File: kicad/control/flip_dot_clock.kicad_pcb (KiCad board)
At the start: 4 copper layers, 140.2 x 46.1 mm, 33 parts, among them U1 NUCLEO-F303K8-HEADER, U10 Small_7_Seg_FlipDot_Module, U2 SLC03B-05, U3 NCV7719, U4 Small_7_Seg_FlipDot_Module, U5 NCV7719, U6 Small_7_Seg_FlipDot_Module, U7 NCV7719, U8 Small_7_Seg_FlipDot_Module, U9 NCV7719

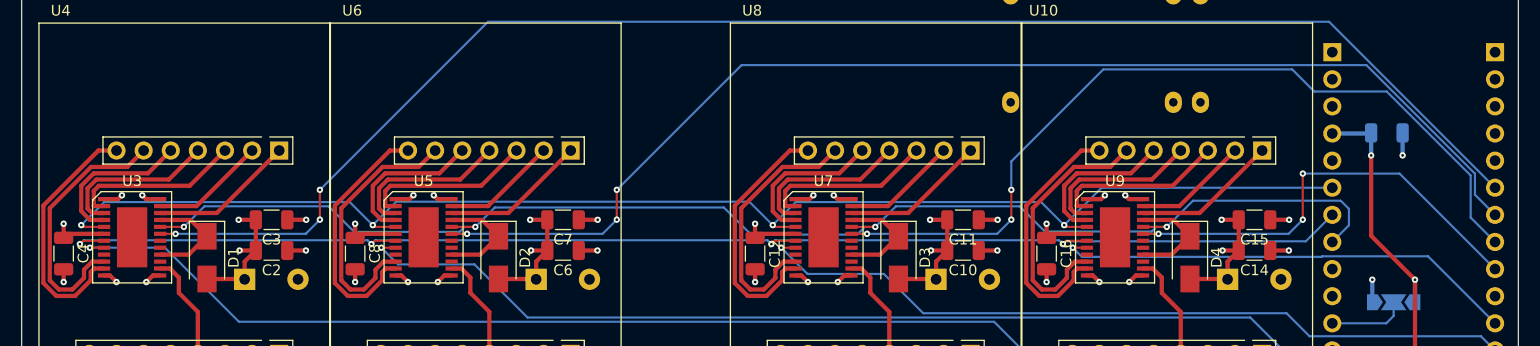
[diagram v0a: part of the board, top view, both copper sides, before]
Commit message: update power planes, move C17, update EN pin mux
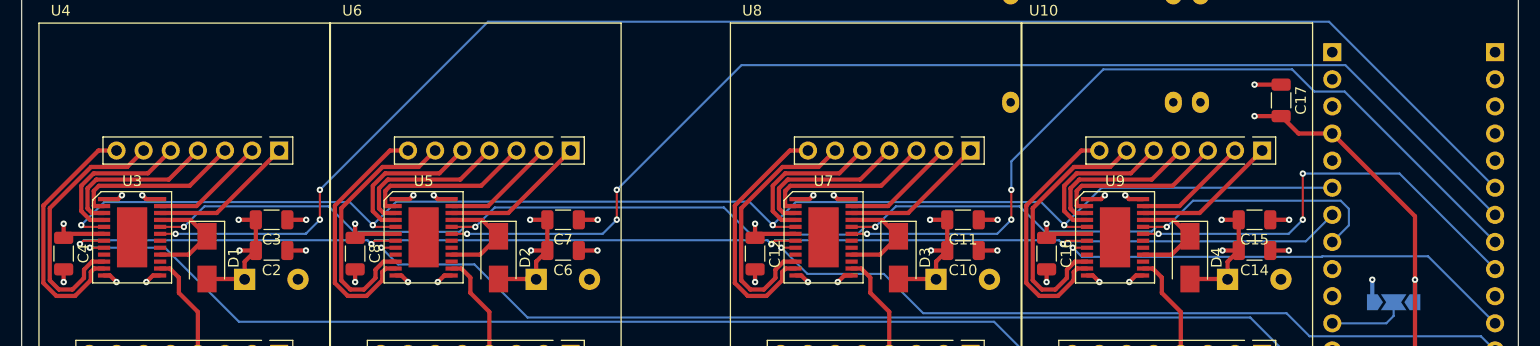
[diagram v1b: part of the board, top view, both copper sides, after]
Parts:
- C17: moved to F.Cu
- moved C17 10.4 mm to (196.7, 86.1), turned to -90 degrees
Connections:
- C17 pad 1: +5V -> GND
- C17 pad 2: GND -> +5V
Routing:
- net +5V: track 54.2 -> 60.0 mm
- net /SPI1_CS_3: track 78.9 -> 76.6 mm
- net /SPI1_CS_2: track 112.9 -> 111.7 mm

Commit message: DRC updates
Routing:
- net /F_SET_1: track 24.8 -> 20.0 mm
- net /F_SET_2: track 24.8 -> 20.0 mm
- net /F_SET_3: track 24.8 -> 20.0 mm
- net /F_SET_4: track 24.8 -> 20.0 mm
- net /G_SET_1: track 23.9 -> 19.2 mm
- net /G_SET_4: track 23.9 -> 19.2 mm
- net /G_SET_3: track 23.9 -> 19.2 mm
- net /G_SET_2: track 23.9 -> 19.2 mm

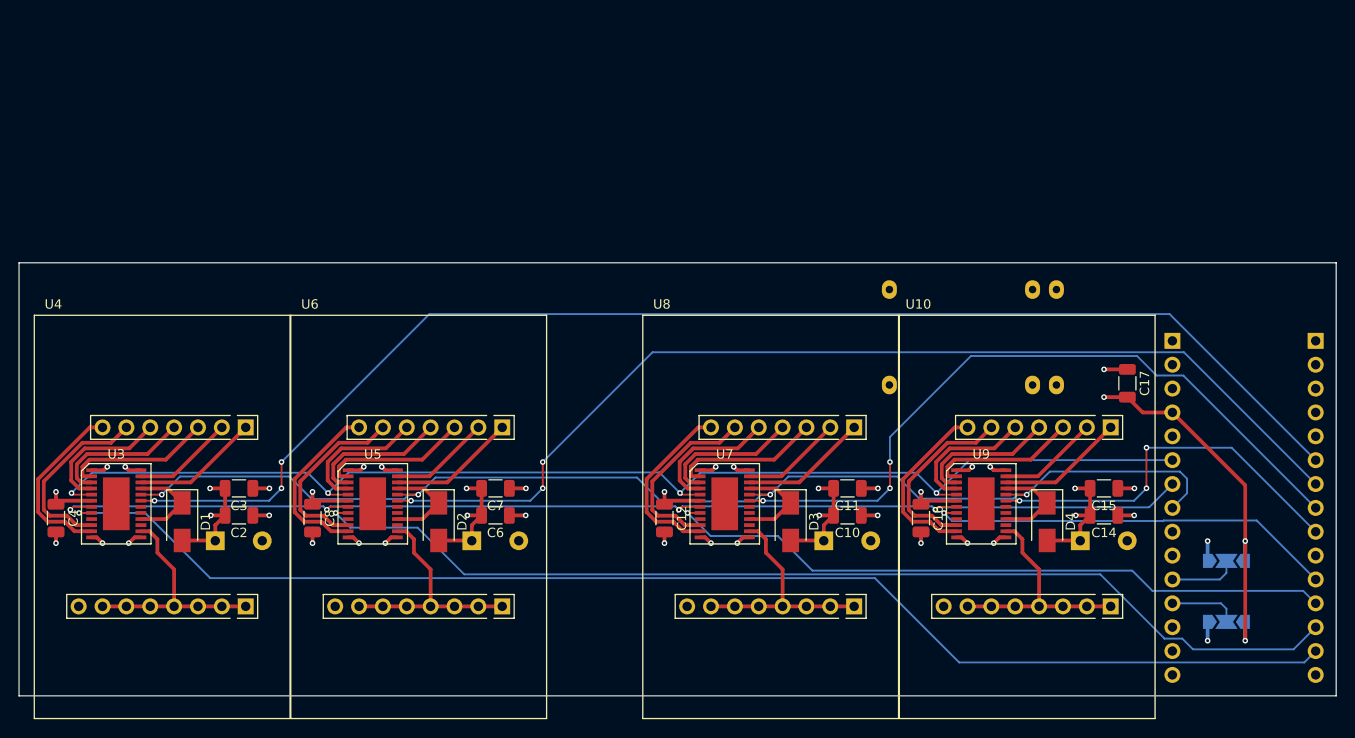
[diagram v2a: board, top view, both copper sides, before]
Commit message: update layout, add power connector
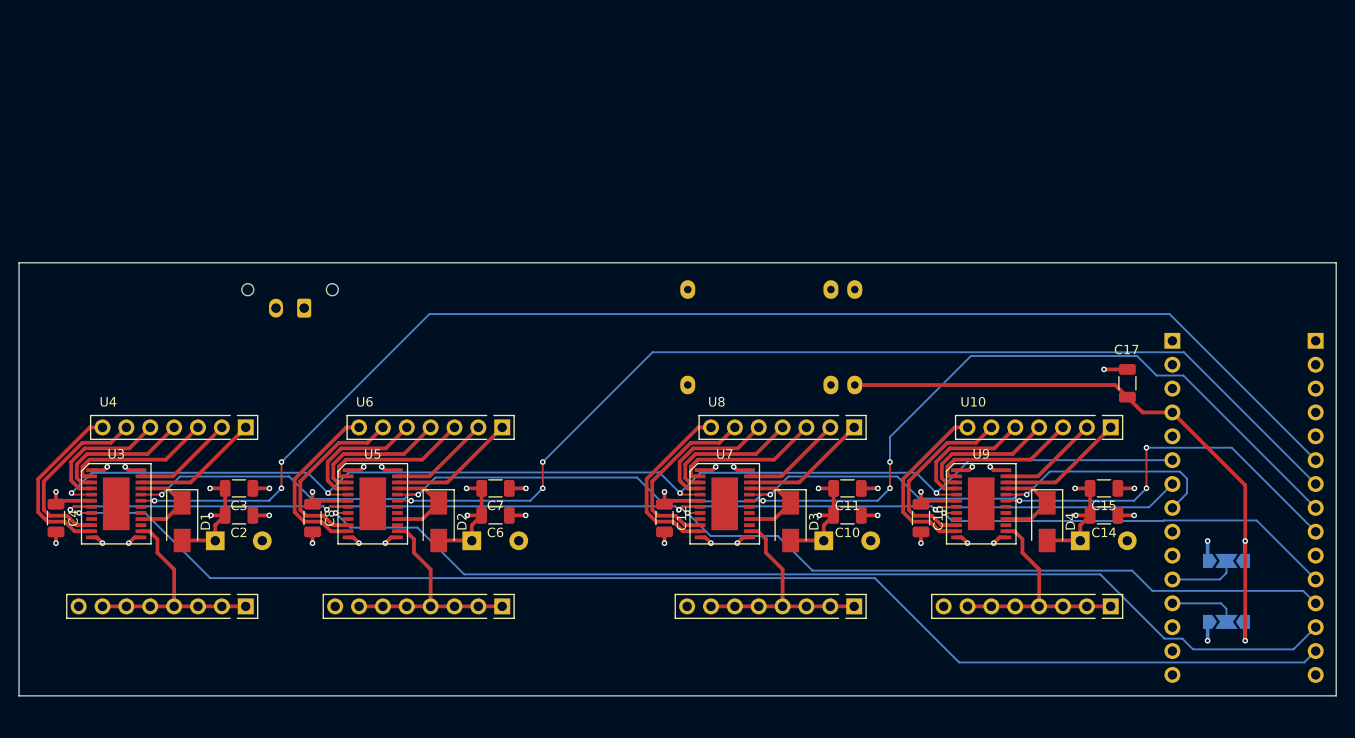
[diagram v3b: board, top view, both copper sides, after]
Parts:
- added J1: Conn_01x02_Male, Connector_Molex:Molex_Micro-Fit_3.0_43650-0215_1x02_P3.00mm_Vertical, B.Cu at (109.1, 78.1)
- moved U2 21.5 mm to (147.8, 74.4)
- turned C17 to 90 degrees
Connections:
- C17 pad 1: GND -> +5V
- C17 pad 2: +5V -> GND
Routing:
- net +5V: track 60.0 -> 87.0 mm, vias 7 -> 6

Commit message: updates
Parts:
- JP1, JP2: value SB -> SJ2O; footprint Jumper:SolderJumper-3_P2.0mm_Open_TrianglePad1.0x1.5mm_NumberLabels -> Jumper:SolderJumper-2_P1.3mm_Open_TrianglePad1.0x1.5mm
- moved JP1 2.69 mm to (209.2, 109.6)
- moved JP2 2.69 mm to (209.2, 106.9)
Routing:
- net +5V: track 87.0 -> 79.3 mm, vias 6 -> 5
- net GND: track 51.9 -> 47.8 mm, vias 31 -> 29
- net /SPI1_SCK: track 129.2 -> 125.8 mm
- net /SPI1_CS_3: track 76.6 -> 74.9 mm
- net /NCV_EN_3: track 72.2 -> 73.7 mm
- net /NCV_EN_2: track 112.7 -> 111.7 mm

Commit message: update pcb
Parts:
- moved J1 0.63 mm to (109.1, 78.7)
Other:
- board size 140.2 x 46.1 mm -> 139.7 x 45.7 mm
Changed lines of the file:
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@@
     )
     (pad_to_mask_clearance 0)
-    (grid_origin 78.74 119.38)
+    (grid_origin 79.248 119.38)
     (pcbplotparams
       (layerselection 0x00010f0_ffffffff)
@@
       (effects (font (size 1 1) (thickness 0.15)))
     )
-    (fp_text value "Small_7_Seg_FlipDot_Module" (at 12.7 -15.875) (layer "F.Fab")
+    (fp_text value "Small_7_Seg_FlipDot_Module" (at 12.573 -4.064) (layer "F.Fab")
       (effects (font (size 1 1) (thickness 0.15)))
     )
@@
       (effects (font (size 1 1) (thickness 0.15)))
     )
-    (fp_text value "Small_7_Seg_FlipDot_Module" (at 12.7 -15.875) (layer "F.Fab")
+    (fp_text value "Small_7_Seg_FlipDot_Module" (at 12.573 -4.064) (layer "F.Fab")
       (effects (font (size 1 1) (thickness 0.15)))
     )
@@
       (effects (font (size 1 1) (thickness 0.15)))
     )
-    (fp_text value "Small_7_Seg_FlipDot_Module" (at 12.7 -15.875) (layer "F.Fab")
+    (fp_text value "Small_7_Seg_FlipDot_Module" (at 12.573 -4.064) (layer "F.Fab")
       (effects (font (size 1 1) (thickness 0.15)))
     )
@@
       (effects (font (size 1 1) (thickness 0.15)))
     )
-    (fp_text value "Small_7_Seg_FlipDot_Module" (at 12.7 -15.875) (layer "F.Fab")
+    (fp_text value "Small_7_Seg_FlipDot_Module" (at 12.7 -4.191) (layer "F.Fab")
       (effects (font (size 1 1) (thickness 0.15)))
     )
@@
   )
   (footprint "Connector_Molex:Molex_Micro-Fit_3.0_43650-0215_1x02_P3.00mm_Vertical" (layer "B.Cu")
-    (at 109.093 78.105 180)
+    (at 109.093 78.74 180)
     (descr "Molex Micro-Fit 3.0 Connector System, 43650-0215 (compatible alternatives: 43650-0216, 43650-0217), 2 Pins per row (http://www.molex.com/pdm_docs/sd/436500215_sd.pdf), generated with kicad-footprint-generator")
     (tags "connector Molex Micro-Fit_3.0 vertical")
@@
     )
   )
-  (gr_line (start 78.74 119.38) (end 78.74 73.279)
+  (gr_line (start 79.248 119.38) (end 79.248 73.66)
     (stroke (width 0.05) (type solid)) (layer "Edge.Cuts"))
-  (gr_line (start 78.74 73.279) (end 218.948 73.279)
+  (gr_line (start 79.248 73.66) (end 218.948 73.66)
     (stroke (width 0.05) (type solid)) (layer "Edge.Cuts"))
-  (gr_line (start 218.948 119.38) (end 78.74 119.38)
+  (gr_line (start 218.948 119.38) (end 79.248 119.38)
     (stroke (width 0.05) (type solid)) (layer "Edge.Cuts"))
-  (gr_line (start 218.948 73.279) (end 218.948 119.38)
+  (gr_line (start 218.948 73.66) (end 218.948 119.38)
     (stroke (width 0.05) (type solid)) (layer "Edge.Cuts"))
+  (dimension (type aligned) (layer "Eco1.User")
+    (pts (xy 79.248 119.38) (xy 218.948 119.38))
+    (height 8.762999)
+    (gr_text "5500.0000  mils" (at 149.098 126.342999) (layer "Eco1.User")
+      (effects (font (size 1.5 1.5) (thickness 0.3)))
+    )
+    (format (units 3) (units_format 1) (precision 4))
+    (style (thickness 0.2) (arrow_length 1.27) (text_position_mode 0) (extension_height 0.58642) (extension_offset 0.5) keep_text_aligned)
+  )
+  (dimension (type aligned) (layer "Eco1.User")
+    (pts (xy 79.248 119.38) (xy 79.248 73.66))
+    (height -6.858)
+    (gr_text "1800.0000  mils" (at 70.59 96.52 90) (layer "Eco1.User")
+      (effects (font (size 1.5 1.5) (thickness 0.3)))
+    )
+    (format (units 3) (units_format 1) (precision 4))
+    (style (thickness 0.2) (arrow_length 1.27) (text_position_mode 0) (extension_height 0.58642) (extension_offset 0.5) keep_text_aligned)
+  )
   (segment (start 96.107 98.838) (end 94.577 97.308) (width 0.4) (layer "F.Cu") (net 1))
   (segment (start 96.107 98.838) (end 94.387 100.558) (width 0.4) (layer "F.Cu") (net 1))
@@
       (pts
         (xy 218.44 118.872)
-        (xy 79.248 118.872)
-        (xy 79.248 73.787)
-        (xy 218.44 73.787)
+        (xy 79.756 118.872)
+        (xy 79.756 74.168)
+        (xy 218.44 74.168)
       )
     )
@@
         (xy 86.106 94.996)
         (xy 86.106 99.441)
-        (xy 79.248 99.441)
-        (xy 79.248 90.043)
+        (xy 79.756 99.441)
+        (xy 79.756 90.043)
         (xy 86.106 90.043)
         (xy 86.106 92.329)
@@
       (pts
         (xy 218.44 118.872)
-        (xy 79.248 118.872)
-        (xy 79.248 100.076)
+        (xy 79.756 118.872)
+        (xy 79.756 100.076)
         (xy 86.741 100.076)
         (xy 86.741 95.631)
@@
         (xy 162.179 82.55)
         (xy 162.179 89.281)
-        (xy 79.248 89.408)
-        (xy 79.248 73.787)
-        (xy 166.751 73.787)
-        (xy 218.44 73.787)
+        (xy 79.756 89.408)
+        (xy 79.756 74.168)
+        (xy 218.44 74.168)
       )
     )

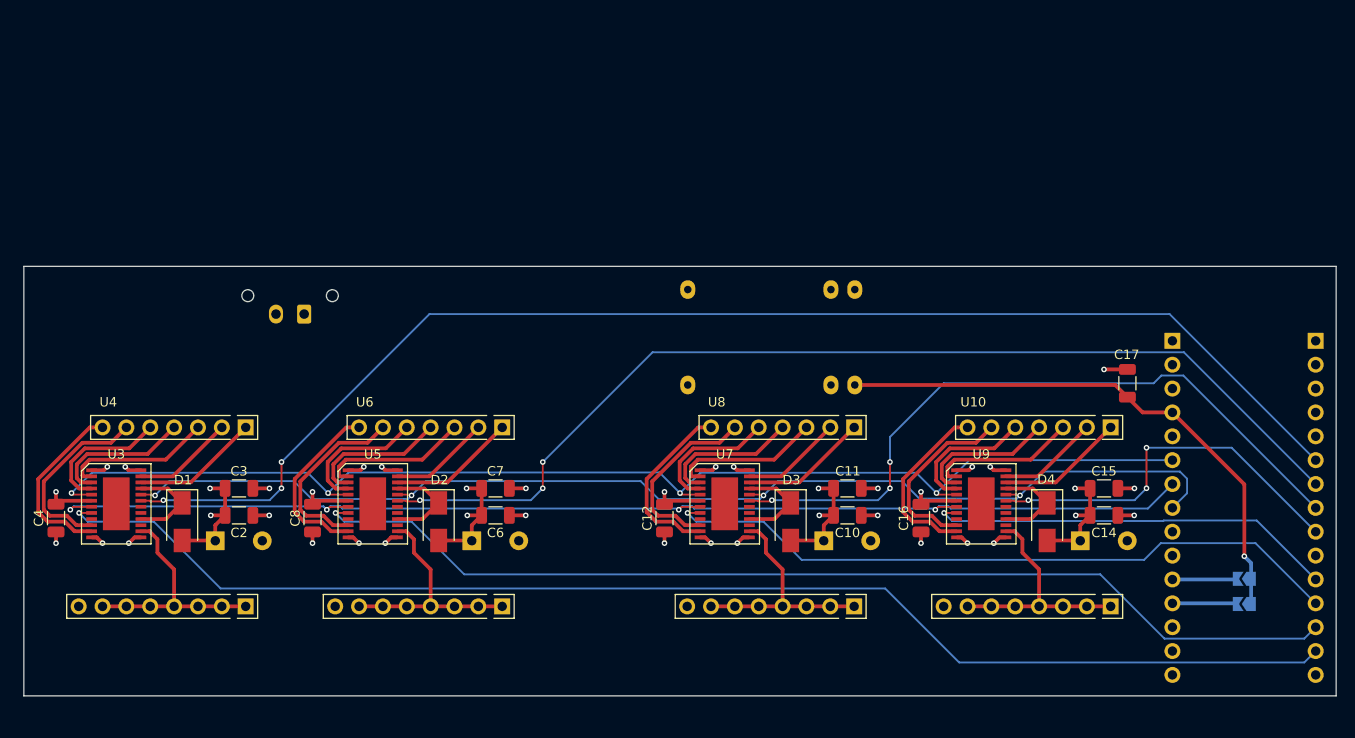
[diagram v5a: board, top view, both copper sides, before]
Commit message: begin PCB redesign based on overall clock dims
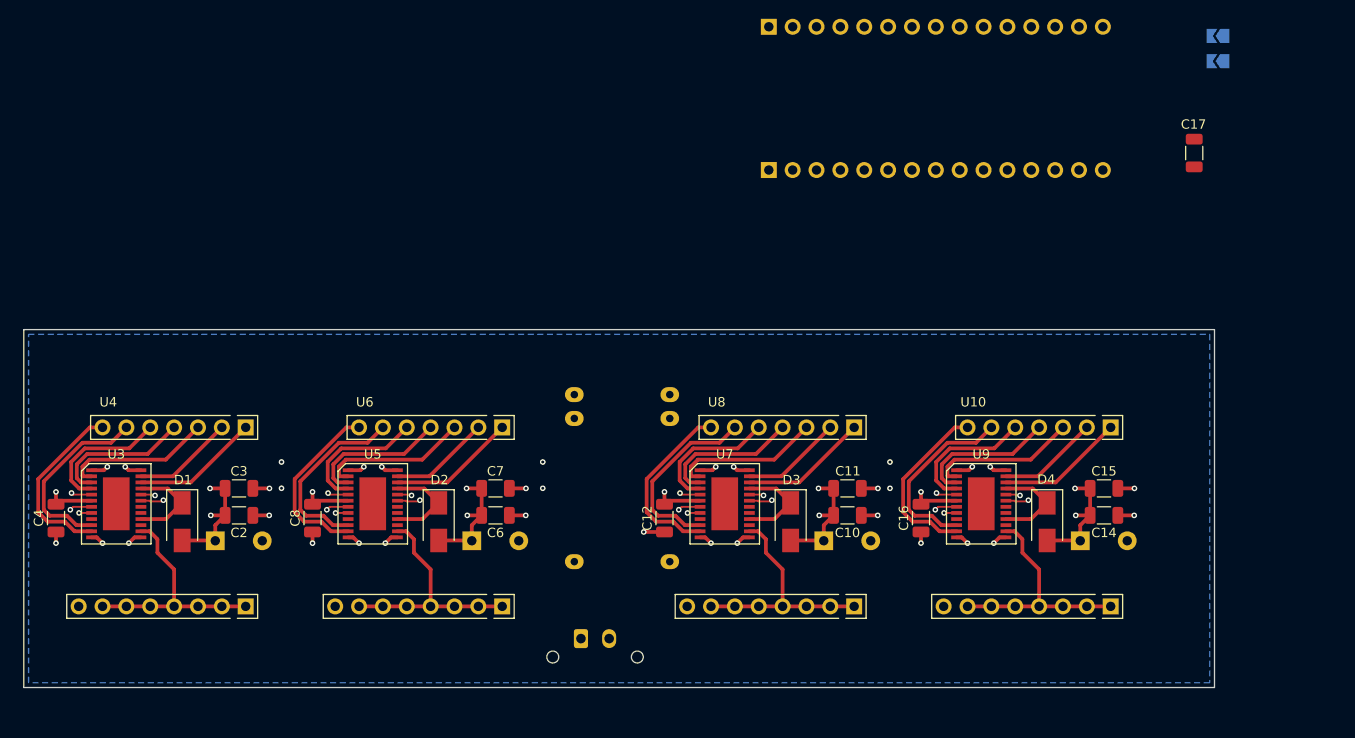
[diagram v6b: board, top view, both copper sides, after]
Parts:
- moved U1 78.9 mm to (200.2, 46.5), turned to -90 degrees
- moved JP2 57.9 mm to (206.4, 49.1)
- moved JP1 57.9 mm to (206.4, 51.8)
- moved J1 45.4 mm to (138.6, 113.3), turned to 0 degrees
- moved U2 34.9 mm to (136.1, 107.3), turned to 90 degrees
- moved C17 25.5 mm to (203.8, 61.6)
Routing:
- net +5V: track 79.3 -> 20.4 mm, vias 5 -> 4
- net /SPI1_CS_1: track 141.4 -> 86.7 mm
- net /SPI1_CS_2: track 111.8 -> 62.2 mm
- net /SPI1_CS_3: track 74.9 -> 26.7 mm
- net /NCV_EN_1: track 140.1 -> 99.4 mm
- net /SPI1_CS_4: track 41.6 -> 16.1 mm, vias 3 -> 1
- net /SPI1_MOSI: track 132.9 -> 115.1 mm
- net /NCV_EN_4: track 43.9 -> 30.8 mm
- net /SPI1_SCK: track 125.8 -> 116.2 mm
- net Net-(JP2-B): track 6.96 -> 0.10 mm
- net Net-(JP1-B): track 6.96 -> 0.10 mm
- net /NCV_EN_3: track 73.7 -> 68.7 mm
- net /SPI1_MISO: track 129.2 -> 131.6 mm
- net GND: track 47.8 -> 46.3 mm, vias 29 -> 28
- net /NCV_EN_2: track 111.7 -> 110.3 mm
- added copper zone on B.Cu, net GND
- removed copper zone on In1.Cu, net GND
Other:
- board size 139.7 x 45.7 mm -> 126.7 x 38.1 mm
